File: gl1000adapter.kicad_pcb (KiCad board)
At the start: 2 copper layers, 31 x 52 mm, 21 parts, among them J1 Barrel_Jack, J2 DB9_Male, J3 DB25_Female, J4 DB9_Male, SW1 SW_SPST

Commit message: Added missing value for R1.
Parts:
- R1: value R -> 5k1
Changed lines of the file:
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@@
     (add_net /LIN1)
     (add_net /LIN2)
+    (add_net /OPT1)
+    (add_net /OPT2)
+    (add_net /OPT3)
+    (add_net /OPT4)
+    (add_net /OPT5)
+    (add_net /OPT6)
     (add_net /RS232RX)
     (add_net /RS232TX)
@@
     (add_net /WAKE)
     (add_net "Net-(D1-Pad1)")
+    (add_net "Net-(J2-Pad1)")
+    (add_net "Net-(J2-Pad4)")
+    (add_net "Net-(J2-Pad5)")
+    (add_net "Net-(J2-Pad8)")
+    (add_net "Net-(J2-Pad9)")
+    (add_net "Net-(J4-Pad1)")
+    (add_net "Net-(J4-Pad4)")
+    (add_net "Net-(J4-Pad5)")
+    (add_net "Net-(J4-Pad8)")
+    (add_net "Net-(J4-Pad9)")
   )
   (module Symbol:KiCad-Logo_5mm_SilkScreen locked (layer B.Cu)
@@
       (effects (font (size 1 1) (thickness 0.15)))
     )
-    (fp_text value R (at 0 1.82 90) (layer F.Fab)
+    (fp_text value 5k1 (at 0 1.82 90) (layer F.Fab)
       (effects (font (size 1 1) (thickness 0.15)))
     )

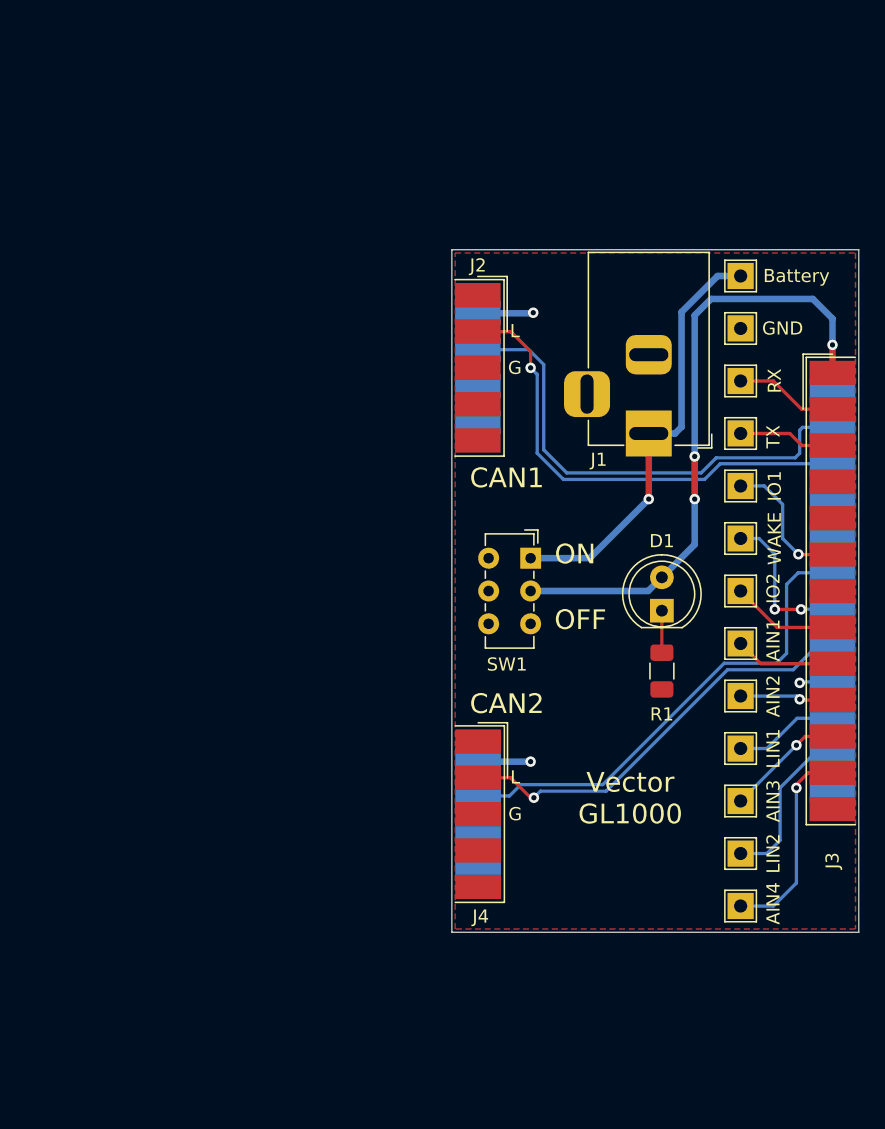
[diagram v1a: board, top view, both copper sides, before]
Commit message: Mayor modifications, added second pair of DB9s, added switchable termination resistors.
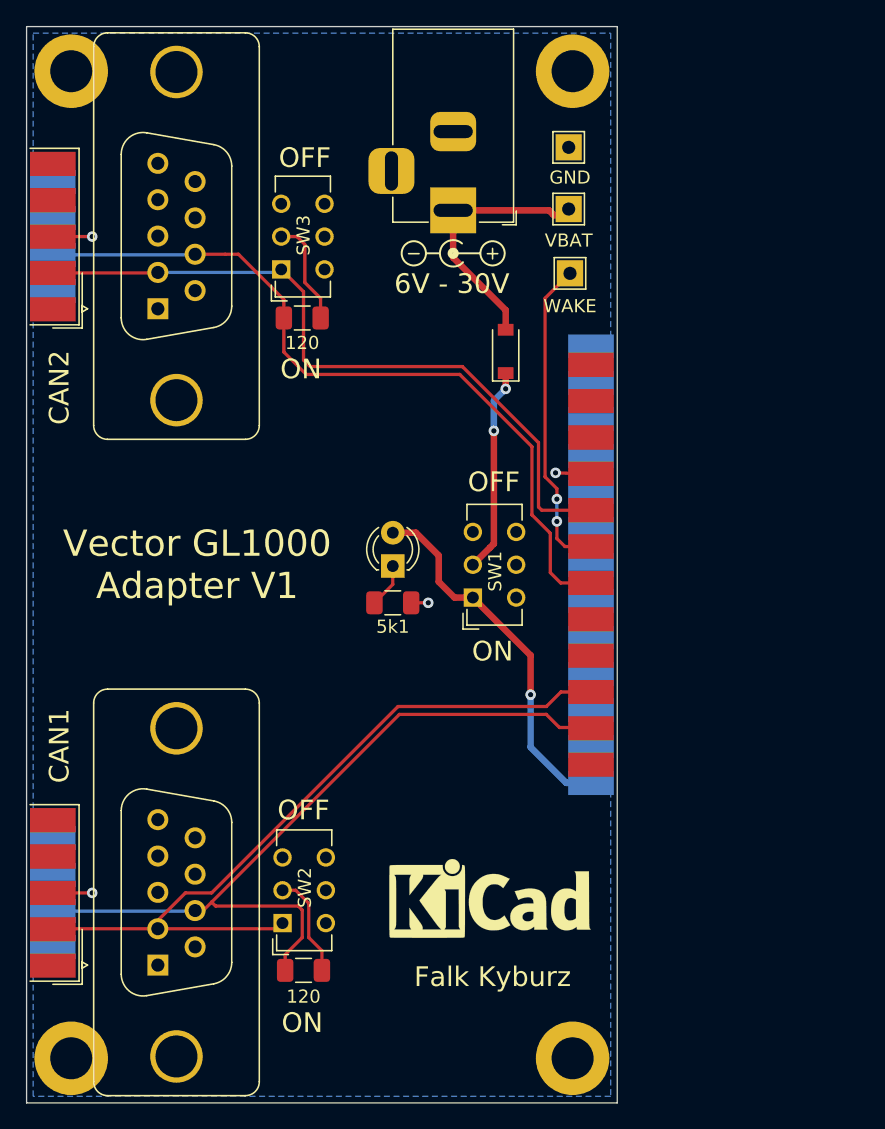
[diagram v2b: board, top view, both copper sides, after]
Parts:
- removed LOGO: KiCad-Logo_5mm_SilkScreen, Symbol:KiCad-Logo_5mm_SilkScreen
- removed TP10: LIN2, TestPoint:TestPoint_THTPad_2.0x2.0mm_Drill1.0mm
- removed TP11: AIN4, TestPoint:TestPoint_THTPad_2.0x2.0mm_Drill1.0mm
- removed TP2: TX, TestPoint:TestPoint_THTPad_2.0x2.0mm_Drill1.0mm
- removed TP3: IO1, TestPoint:TestPoint_THTPad_2.0x2.0mm_Drill1.0mm
- removed TP4: WAKE, TestPoint:TestPoint_THTPad_2.0x2.0mm_Drill1.0mm
- removed TP5: IO2, TestPoint:TestPoint_THTPad_2.0x2.0mm_Drill1.0mm
- removed TP6: AIN1, TestPoint:TestPoint_THTPad_2.0x2.0mm_Drill1.0mm
- removed TP7: AIN2, TestPoint:TestPoint_THTPad_2.0x2.0mm_Drill1.0mm
- removed TP8: LIN1, TestPoint:TestPoint_THTPad_2.0x2.0mm_Drill1.0mm
- removed TP9: AIN3, TestPoint:TestPoint_THTPad_2.0x2.0mm_Drill1.0mm
- added D2: SM4007PL, Diode_SMD:D_SOD-123, F.Cu at (141.5, 78.8)
- added J5: DS1034-09MUNSi44, Connector_Dsub:DSUB-9_Male_Vertical_P2.77x2.84mm_MountingHoles, F.Cu at (115.0, 125.5)
- added J6: DS1034-09MUNSi44, Connector_Dsub:DSUB-9_Male_Vertical_P2.77x2.84mm_MountingHoles, F.Cu at (115.0, 75.5)
- added R2: 120, Resistor_SMD:R_1206_3216Metric, F.Cu at (126.1, 125.9)
- added R3: 120, Resistor_SMD:R_1206_3216Metric, F.Cu at (126.0, 76.2)
- added REF**: MountingHole_3.2mm_M3_DIN965_Pad, MountingHole:MountingHole_3.2mm_M3_DIN965_Pad, F.Cu at (146.6, 57.4)
- added REF**: MountingHole_3.2mm_M3_DIN965_Pad, MountingHole:MountingHole_3.2mm_M3_DIN965_Pad, F.Cu at (146.6, 132.6)
- added REF**: MountingHole_3.2mm_M3_DIN965_Pad, MountingHole:MountingHole_3.2mm_M3_DIN965_Pad, F.Cu at (108.4, 57.4)
- added REF**: MountingHole_3.2mm_M3_DIN965_Pad, MountingHole:MountingHole_3.2mm_M3_DIN965_Pad, F.Cu at (108.4, 132.6)
- added REF**: KiCad-Logo_6mm_SilkScreen, Symbol:KiCad-Logo_6mm_SilkScreen, F.Cu at (140.3, 120.4)
- added REF**: OSHW-Logo2_9.8x8mm_SilkScreen, Symbol:OSHW-Logo2_9.8x8mm_SilkScreen, B.Cu at (120.5, 96.1)
- added REF**: Symbol_Barrel_Polarity, Symbol:Symbol_Barrel_Polarity, F.Cu at (137.5, 71.2)
- added SW2: K3-2235D-K1, Button_Switch_THT:SW_CuK_JS202011CQN_DPDT_Straight, F.Cu at (124.5, 122.3)
- added SW3: K3-2235D-K1, Button_Switch_THT:SW_CuK_JS202011CQN_DPDT_Straight, F.Cu at (124.4, 72.5)
- D1: value LED -> LED 3mm green; footprint LED_THT:LED_D5.0mm -> LED_THT:LED_D3.0mm
- J2, J4: value DB9_Male -> DS1033-09FUNSiSS; footprint Connector_Dsub:DSUB-9_Male_EdgeMount_P2.77mm -> Connector_Dsub:DSUB-9_Female_EdgeMount_P2.77mm
- J3: moved to B.Cu
- SW1: value SW_SPST -> K3-2235D-K1; footprint Button_Switch_THT:SW_E-Switch_EG1271_DPDT -> Button_Switch_THT:SW_CuK_JS202011CQN_DPDT_Straight
- TP1: value RX -> WAKE
- TP12: value Battery -> VBAT
- moved J4 54.6 mm to (107.0, 70.0)
- moved J2 51.5 mm to (107.0, 120.0)
- moved J1 22.6 mm to (137.5, 68.0)
- moved R1 21.1 mm to (132.9, 97.9), turned to 0 degrees
- moved D1 20.8 mm to (132.9, 95.1)
- moved TP13 19.0 mm to (146.3, 63.2)
- moved J3 18.5 mm to (148.0, 95.0), turned to 270 degrees
- moved TP1 15.4 mm to (146.4, 72.8)
- moved TP12 14.1 mm to (146.3, 67.9)
- moved SW1 5.33 mm to (139.0, 97.5), turned to 90 degrees
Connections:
- D1 pad 2: /Battery -> /VBAT2
- J3 pad 1: /Battery -> /VBAT2
- J3 pad 10: /AIN2 -> (no net)
- J3 pad 11: /AIN3 -> (no net)
- J3 pad 12: /AIN4 -> (no net)
- J3 pad 2: /RS232RX -> (no net)
- J3 pad 23: /LIN1 -> (no net)
- J3 pad 24: /LIN2 -> (no net)
- J3 pad 3: /RS232TX -> (no net)
- J3 pad 6: /IO1 -> (no net)
- J3 pad 8: /IO2 -> (no net)
- J3 pad 9: /AIN1 -> (no net)
- SW1 pad 1: /VBAT -> /VBAT2
- SW1 pad 2: /Battery -> /VBAT1
- TP1 pad 1: /RS232RX -> /WAKE
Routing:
- net /Battery: track 47.2 -> 0.00 mm, vias 3 -> 0
- net /VBAT2: track 0.00 -> 28.3 mm, vias 0 -> 1
- net /CAN1H: track 37.2 -> 59.9 mm
- net /CAN2L: track 32.4 -> 54.6 mm, vias 1 -> 0
- net /CAN1L: track 36.4 -> 58.5 mm, vias 1 -> 0
- net /CAN2H: track 37.1 -> 59.0 mm
- net /VBAT1: track 0.00 -> 15.6 mm, vias 0 -> 2
- net /AIN4: track 15.6 -> 0.00 mm, vias 1 -> 0
- net /VBAT: track 33.0 -> 18.6 mm, vias 1 -> 0
- net /WAKE: track 11.7 -> 24.2 mm
- net /LIN2: track 12.5 -> 0.00 mm
- net /IO1: track 10.7 -> 0.00 mm, vias 1 -> 0
- net /AIN3: track 9.04 -> 0.00 mm, vias 1 -> 0
- net /IO2: track 8.15 -> 0.00 mm
- net Net-(R3-Pad2): track 0.00 -> 8.15 mm
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- added copper zone on B.Cu, net /GND
- removed copper zone on F.Cu, net /GND
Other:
- board size 31 x 52 mm -> 45 x 82 mm
- net class Power added: clearance 0.2, trace_width 0.5, via_dia 0.8, via_drill 0.4
- board text added: "6V - 30V"
- board text added: "Vector GL1000 Adapter V1"
- board text added: "github.com/falkkyburz/gl1000adapter"
- board text removed: "Center Positive"
- board text removed: "G"
- board text removed: "H"
- board text removed: "L"
- board text removed: "Vector GL1000"

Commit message: Data as ordered.
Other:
- net class Default removed
- net class Power removed
